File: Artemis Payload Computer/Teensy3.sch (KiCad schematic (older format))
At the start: 1 part, among them U201 Teensy3.2

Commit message: complete redo hehe
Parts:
- renumbered U201 to U?
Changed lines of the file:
@@
 $Descr A4 11693 8268
 encoding utf-8
-Sheet 2 5
+Sheet 3 6
 Title ""
 Date ""
@@
 $EndDescr
 $Comp
-L Artemis_Footprints:Teensy3.2 U201
+L Artemis_Footprints:Teensy3.2 U?
 U 1 1 6028516C
 P 6350 3600
-F 0 "U201" H 6350 5343 60  0000 C CNN
+F 0 "U?" H 6350 5343 60  0000 C CNN
 F 1 "Teensy3.2" H 6350 5237 60  0000 C CNN
 F 2 "Artemis Payload Computer:Teensy30_31_32_LC" H 6350 5131 60  0000 C CNN

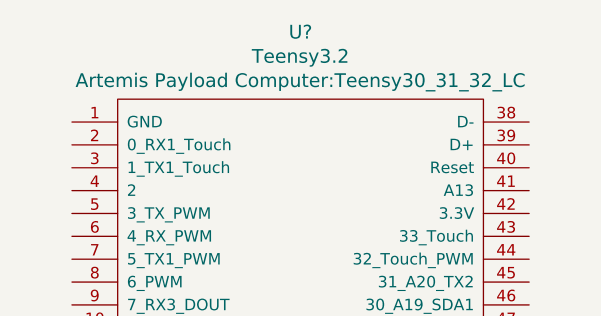
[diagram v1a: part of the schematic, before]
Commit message: Updated Footprints
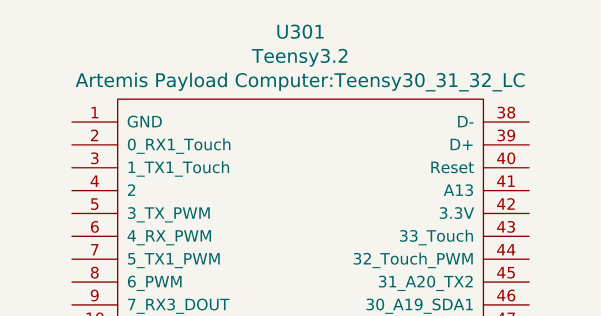
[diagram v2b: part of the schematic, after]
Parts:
- gave numbers to parts that had none: 1
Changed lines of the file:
@@
 $EndDescr
 $Comp
-L Artemis_Footprints:Teensy3.2 U?
+L Artemis_Footprints:Teensy3.2 U301
 U 1 1 6028516C
 P 6350 3600
-F 0 "U?" H 6350 5343 60  0000 C CNN
+F 0 "U301" H 6350 5343 60  0000 C CNN
 F 1 "Teensy3.2" H 6350 5237 60  0000 C CNN
 F 2 "Artemis Payload Computer:Teensy30_31_32_LC" H 6350 5131 60  0000 C CNN

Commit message: ready for testing...
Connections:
- net GND: now reaches U301.1 (GND)
- net GND: now also U301.17 (GND), U301.32 (AGND)
- net SDA0: now reaches U301.25 (18_A4_SDA0_Touch)
- net SCL0: now reaches U301.26 (19_A5_SCL0_Touch)
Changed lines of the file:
@@
 	1    0    0    -1
 $EndComp
+$Comp
+L power:GND #PWR0106
+U 1 1 60404CA5
+P 5000 2250
+F 0 "#PWR0106" H 5000 2000 50  0001 C CNN
+F 1 "GND" V 5005 2122 50  0000 R CNN
+F 2 "" H 5000 2250 50  0001 C CNN
+F 3 "" H 5000 2250 50  0001 C CNN
+	1    5000 2250
+	0    1    1    0
+$EndComp
+$Comp
+L power:GND #PWR0107
+U 1 1 604051D4
+P 5000 3850
+F 0 "#PWR0107" H 5000 3600 50  0001 C CNN
+F 1 "GND" V 5005 3722 50  0000 R CNN
+F 2 "" H 5000 3850 50  0001 C CNN
+F 3 "" H 5000 3850 50  0001 C CNN
+	1    5000 3850
+	0    1    1    0
+$EndComp
+$Comp
+L power:GND #PWR0108
+U 1 1 6040567B
+P 7600 4650
+F 0 "#PWR0108" H 7600 4400 50  0001 C CNN
+F 1 "GND" V 7605 4522 50  0000 R CNN
+F 2 "" H 7600 4650 50  0001 C CNN
+F 3 "" H 7600 4650 50  0001 C CNN
+	1    7600 4650
+	0    -1   -1   0
+$EndComp
+Wire Wire Line
+	7600 4650 7350 4650
+Wire Wire Line
+	5000 3850 5350 3850
+Wire Wire Line
+	5350 2250 5000 2250
+Text HLabel 5000 4750 0    50   Input ~ 0
+SCL0
+Text HLabel 5000 4650 0    50   Input ~ 0
+SDA0
+Wire Wire Line
+	5350 4650 5000 4650
+Wire Wire Line
+	5350 4750 5000 4750
 $EndSCHEMATC

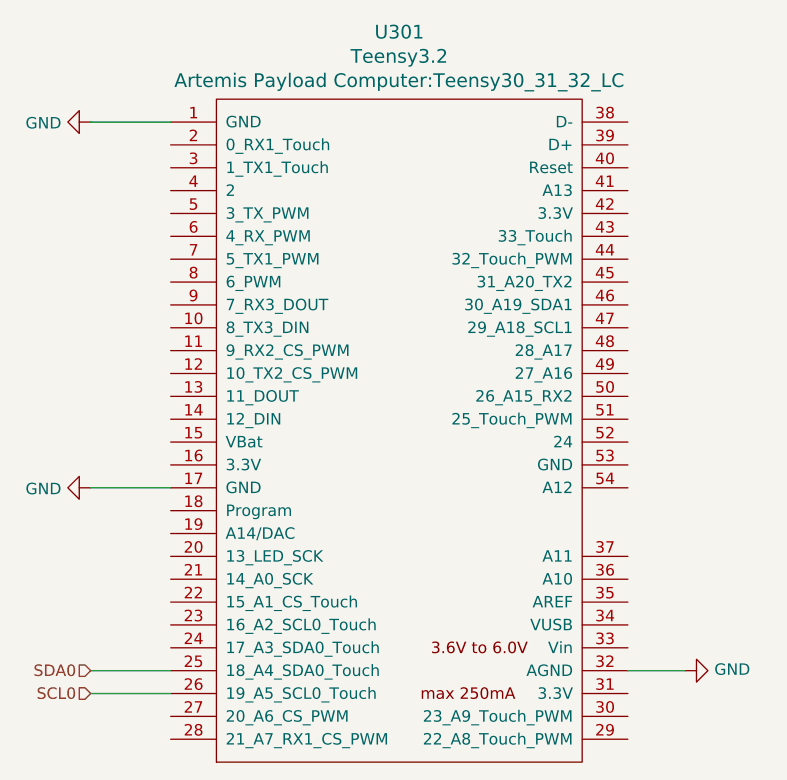
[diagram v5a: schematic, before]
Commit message: Continued work on SD card. Starting PCB layout.
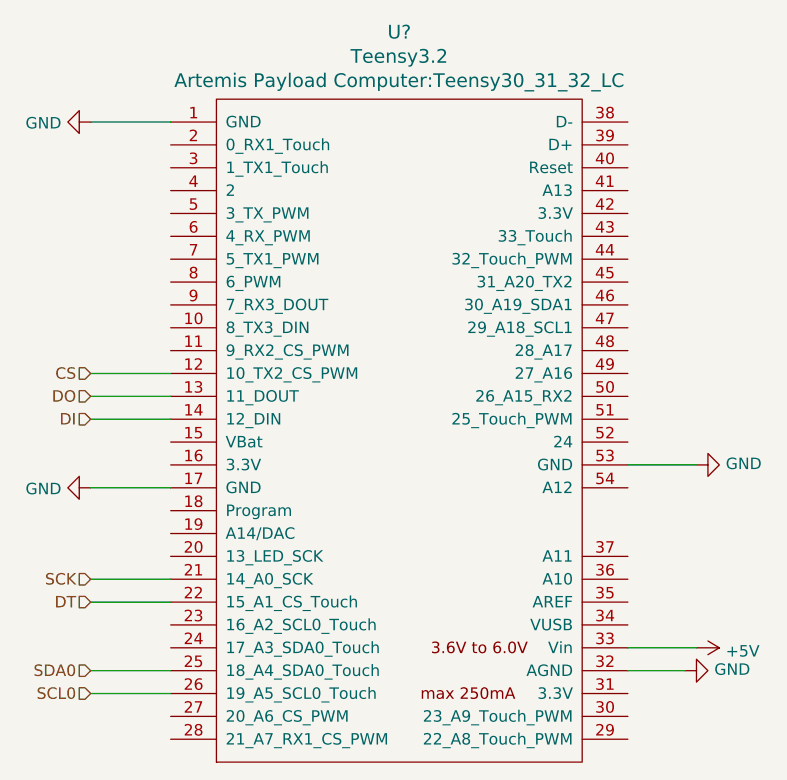
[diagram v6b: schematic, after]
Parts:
- renumbered U301 to U?
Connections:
- net GND: now also U?.53 (GND)
- net CS: now reaches U?.12 (10_TX2_CS_PWM)
- net DO: now reaches U?.13 (11_DOUT)
- net DI: now reaches U?.14 (12_DIN)
- net SCK: now reaches U?.21 (14_A0_SCK)
- net DT: now reaches U?.22 (15_A1_CS_Touch)
- net +5V: now reaches U?.33 (Vin)
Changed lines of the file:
@@
 $EndDescr
 $Comp
-L Artemis_Footprints:Teensy3.2 U301
+L Artemis_Footprints:Teensy3.2 U?
 U 1 1 6028516C
 P 6350 3600
-F 0 "U301" H 6350 5343 60  0000 C CNN
+F 0 "U?" H 6350 5343 60  0000 C CNN
 F 1 "Teensy3.2" H 6350 5237 60  0000 C CNN
 F 2 "Artemis Payload Computer:Teensy30_31_32_LC" H 6350 5131 60  0000 C CNN
@@
 $EndComp
 $Comp
-L power:GND #PWR0106
+L power:GND #PWR?
 U 1 1 60404CA5
 P 5000 2250
-F 0 "#PWR0106" H 5000 2000 50  0001 C CNN
+F 0 "#PWR?" H 5000 2000 50  0001 C CNN
 F 1 "GND" V 5005 2122 50  0000 R CNN
 F 2 "" H 5000 2250 50  0001 C CNN
@@
 $EndComp
 $Comp
-L power:GND #PWR0107
+L power:GND #PWR?
 U 1 1 604051D4
 P 5000 3850
-F 0 "#PWR0107" H 5000 3600 50  0001 C CNN
+F 0 "#PWR?" H 5000 3600 50  0001 C CNN
 F 1 "GND" V 5005 3722 50  0000 R CNN
 F 2 "" H 5000 3850 50  0001 C CNN
@@
 $EndComp
 $Comp
-L power:GND #PWR0108
+L power:GND #PWR?
 U 1 1 6040567B
 P 7600 4650
-F 0 "#PWR0108" H 7600 4400 50  0001 C CNN
+F 0 "#PWR?" H 7600 4400 50  0001 C CNN
 F 1 "GND" V 7605 4522 50  0000 R CNN
 F 2 "" H 7600 4650 50  0001 C CNN
@@
 Wire Wire Line
 	5350 4750 5000 4750
+$Comp
+L power:+5V #PWR?
+U 1 1 6047F910
+P 7650 4550
+F 0 "#PWR?" H 7650 4400 50  0001 C CNN
+F 1 "+5V" V 7665 4678 50  0000 L CNN
+F 2 "" H 7650 4550 50  0001 C CNN
+F 3 "" H 7650 4550 50  0001 C CNN
+	1    7650 4550
+	0    1    1    0
+$EndComp
+Wire Wire Line
+	7650 4550 7350 4550
+$Comp
+L power:GND #PWR?
+U 1 1 6047FEAC
+P 7650 3750
+F 0 "#PWR?" H 7650 3500 50  0001 C CNN
+F 1 "GND" V 7655 3622 50  0000 R CNN
+F 2 "" H 7650 3750 50  0001 C CNN
+F 3 "" H 7650 3750 50  0001 C CNN
+	1    7650 3750
+	0    -1   -1   0
+$EndComp
+Wire Wire Line
+	7650 3750 7350 3750
+Text HLabel 5000 3450 0    50   Input ~ 0
+DO
+Text HLabel 5000 3550 0    50   Input ~ 0
+DI
+Text HLabel 5000 3350 0    50   Input ~ 0
+CS
+Wire Wire Line
+	5350 3350 5000 3350
+Wire Wire Line
+	5000 3450 5350 3450
+Wire Wire Line
+	5350 3550 5000 3550
+Text HLabel 5000 4250 0    50   Input ~ 0
+SCK
+Wire Wire Line
+	5000 4250 5350 4250
+Text HLabel 5000 4350 0    50   Input ~ 0
+DT
+Wire Wire Line
+	5000 4350 5350 4350
 $EndSCHEMATC
